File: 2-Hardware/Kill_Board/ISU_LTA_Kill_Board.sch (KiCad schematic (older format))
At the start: 34 parts, among them P1 CONN_01X02, P10 CONN_2, P11 CONN_2, P12 CONN_2, P13 CONN_2, P2 CONN_01X02, P3 CONN_01X02, P4 CONN_01X03, P5 CONN_01X03, P6 CONN_01X03, P7 CONN_01X03, Q1 NMOS+PMOS, Q2 N-CH, Q3 N-CH, U1 ADAFRUIT_FEATHER, U2 LM2937, U3 SPX2920T-5.0_TO263

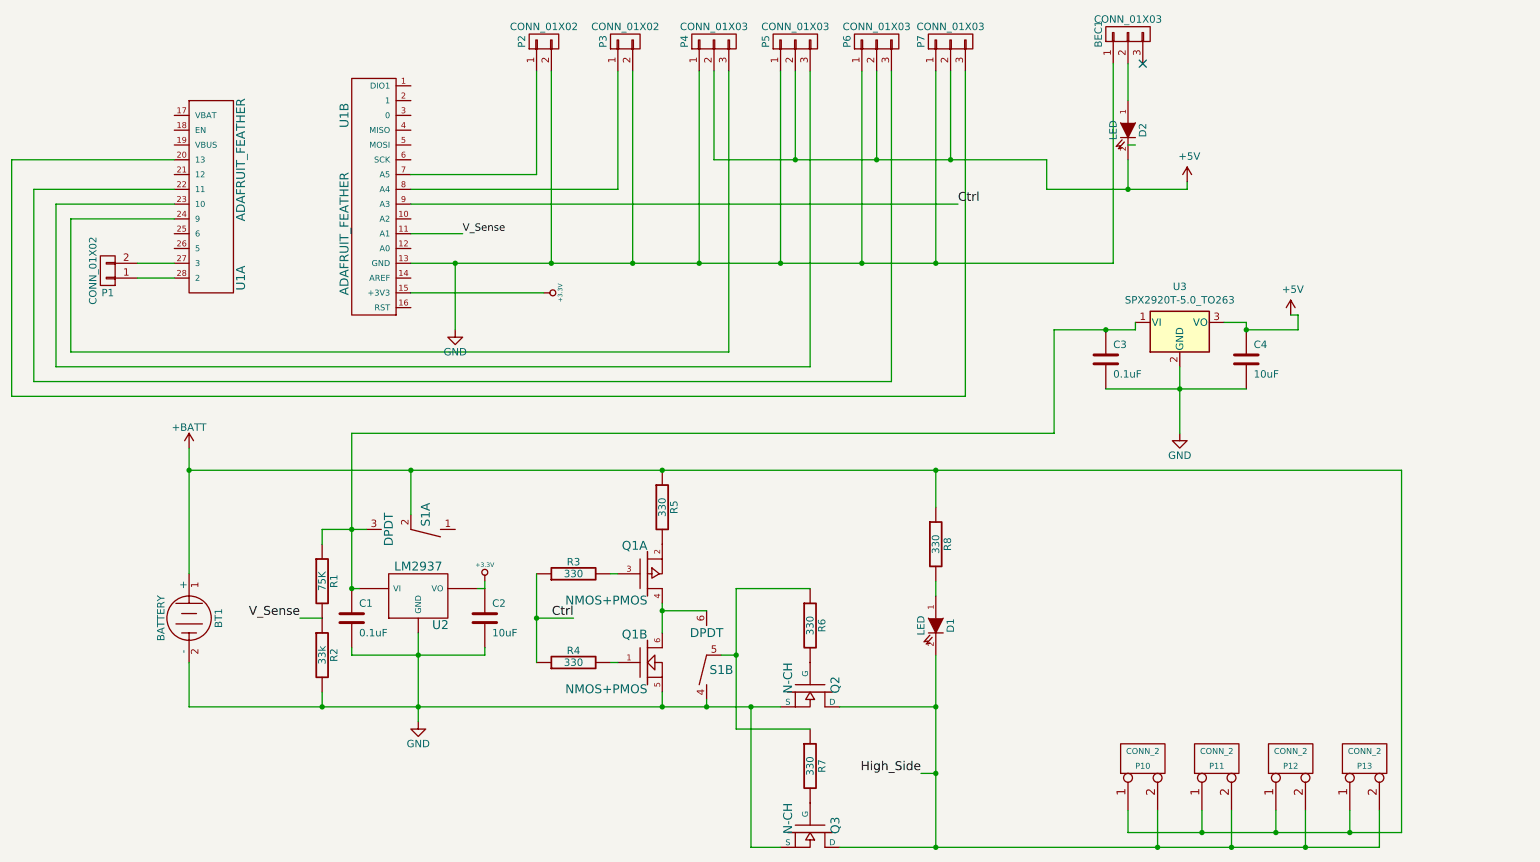
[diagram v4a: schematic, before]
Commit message: Updated to have BEC and level shifter
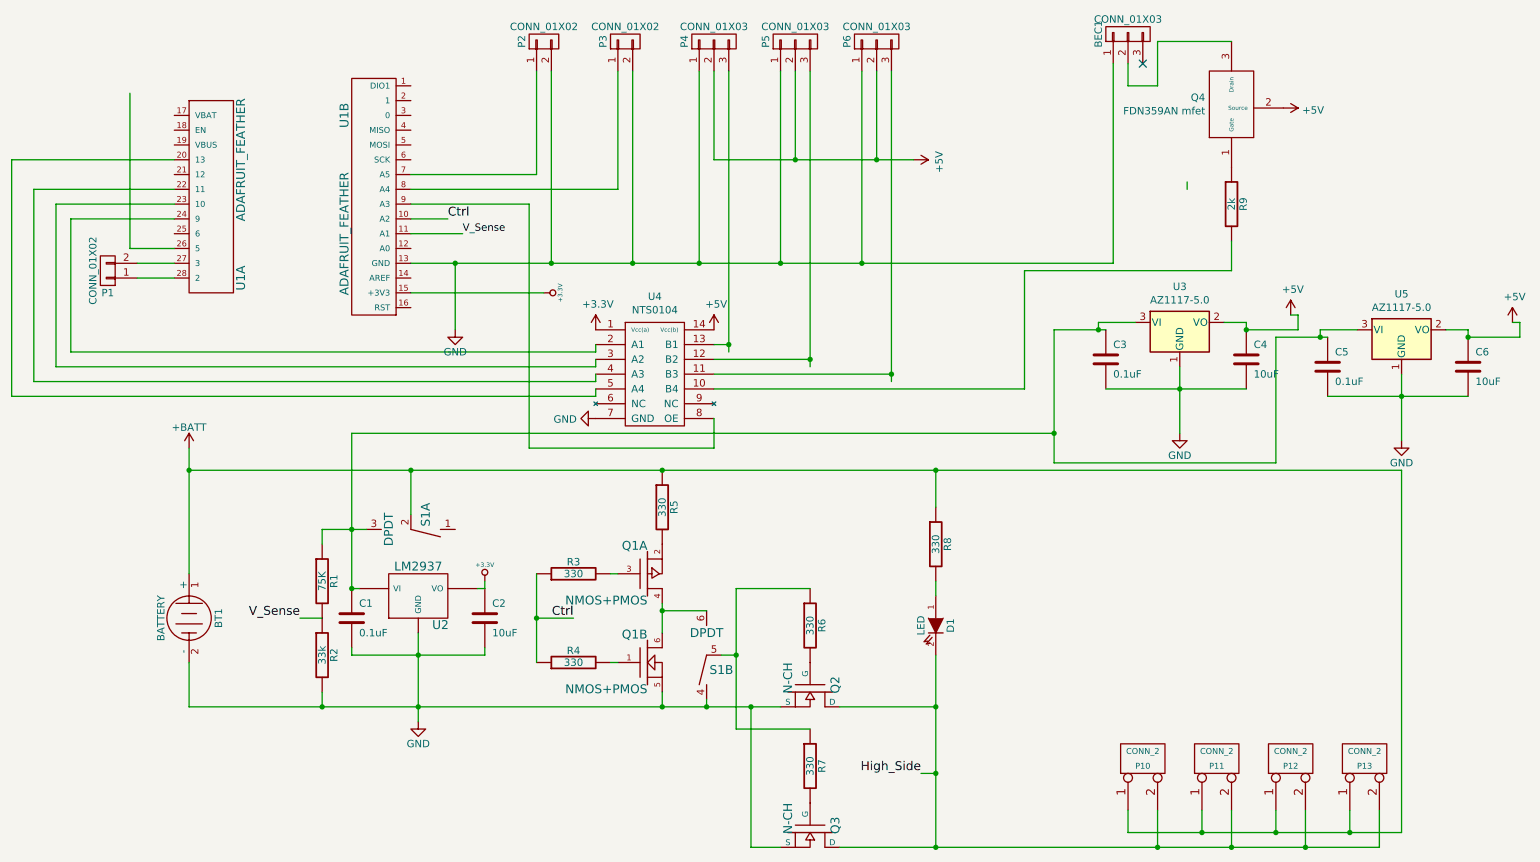
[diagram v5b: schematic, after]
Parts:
- removed D2: LED, LEDs:LED_0805_HandSoldering, symbol ISU_LTA_Kill_Board-rescue:LED-RESCUE-ISU_LTA_Kill_Board
- removed P7: CONN_01X03, Pin_Headers:Pin_Header_Angled_1x03_Pitch2.54mm, symbol ISU_LTA_Kill_Board-rescue:CONN_01X03
- removed U3: SPX2920T-5.0_TO263, TO_SOT_Packages_SMD:TO-263-3_TabPin2, symbol Regulator_Linear:SPX2920T-5.0_TO263
- added C5: 0.1uF, Capacitors_SMD:C_0805_HandSoldering, symbol ISU_LTA_Kill_Board-rescue:C-RESCUE-ISU_LTA_Kill_Board
- added C6: 10uF, Capacitors_SMD:C_0805_HandSoldering, symbol ISU_LTA_Kill_Board-rescue:C-RESCUE-ISU_LTA_Kill_Board
- added Q4: FDN359AN mfet, TO_SOT_Packages_SMD:SOT-23, symbol ISU_LTA_Kill_Board:mosfet
- added R9: 2k, Resistors_SMD:R_0805_HandSoldering, symbol ISU_LTA_Kill_Board-rescue:R-RESCUE-ISU_LTA_Kill_Board
- added U3, U5: AZ1117-5.0, TO_SOT_Packages_SMD:SOT-223-3_TabPin2, symbol Regulator_Linear:AZ1117-5.0
- added U4: NTS0104, Housings_SSOP:TSSOP-14_4.4x5mm_Pitch0.65mm, symbol ISU_LTA_Kill_Board:NTS0104
- BT1: footprint Connector_Wire:SolderWirePad_1x02_P7.62mm_Drill2.5mm -> Adafruit:SolderWirePad_2x_2-5mmDrill
- Q1: footprint Package_TO_SOT_SMD:SOT-23-6_Handsoldering -> TO_SOT_Packages_SMD:SOT-23-6
- Q2, Q3: footprint Package_TO_SOT_SMD:TO-263-3_TabPin2 -> TO_SOT_Packages_SMD:TO-263-3_TabPin2
- S1: footprint Button_Switch_THT:SW_CuK_JS202011CQN_DPDT_Straight -> Buttons_Switches_ThroughHole:SW_CuK_JS202011CQN_DPDT_Straight
- U2: footprint Package_TO_SOT_SMD:SOT-223 -> TO_SOT_Packages_SMD:SOT-223
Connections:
- wire segments 143 -> 173
